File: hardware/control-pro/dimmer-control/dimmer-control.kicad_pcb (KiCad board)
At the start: 2 copper layers, 100 x 90 mm, 20 parts, among them J1 OUTPUT, J2 INPUT

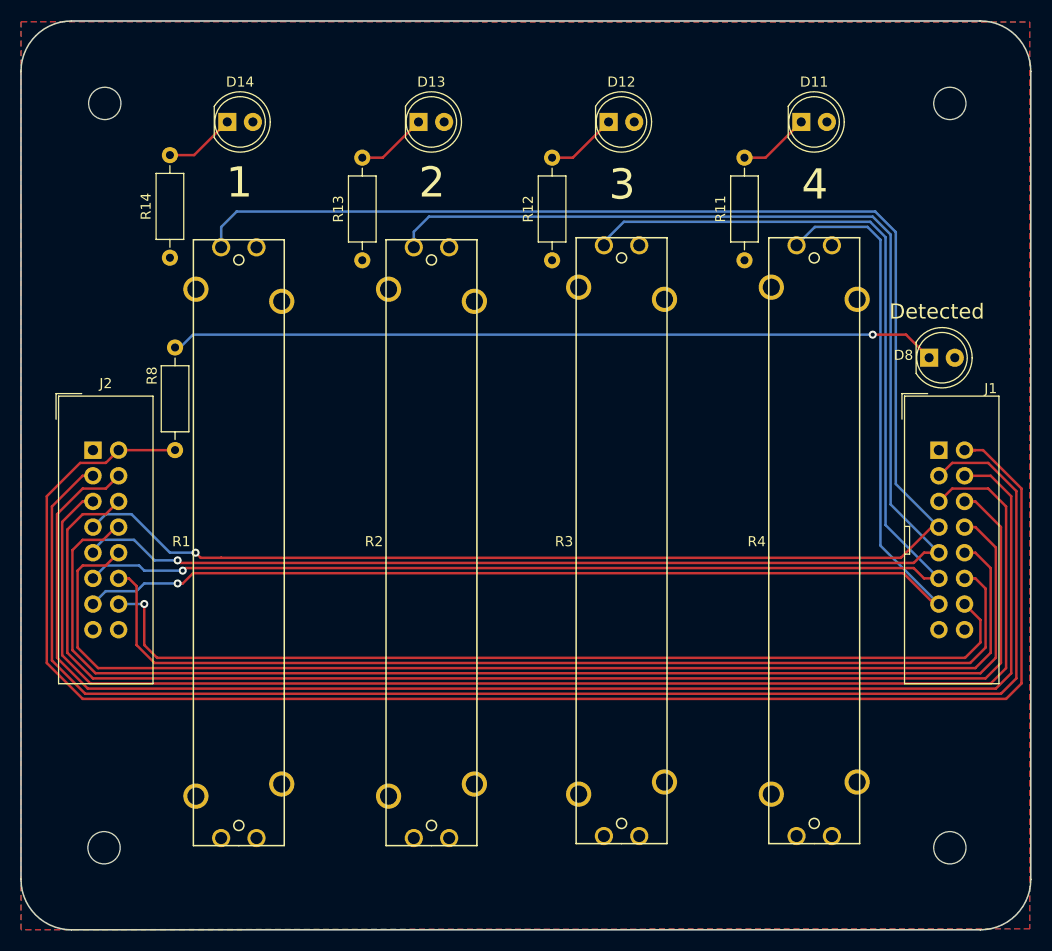
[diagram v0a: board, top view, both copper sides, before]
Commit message: TX2: - Added buffer to drive LEDs - Added decoupling capacitors - Fixed dimmer traces on PCB
DMX-CPC*:
- Switched to horizontal 16 pin connectors since vertical was too tall with a cable plugged in
- Swapped the clock speed and step switches to match the order on the TX1
- Swapped the data and clock LEDs to match the order on the TX1

DMX-CPD*:
- Split dimmer controls out to its own PCB
- Added 2nd 16 pin connector to daisy chain with DMX-CPC*.
- Switched to horizontal 16 pin connectors since vertical was too tall with a cable plugged in

Updated readmes with parts, board links.
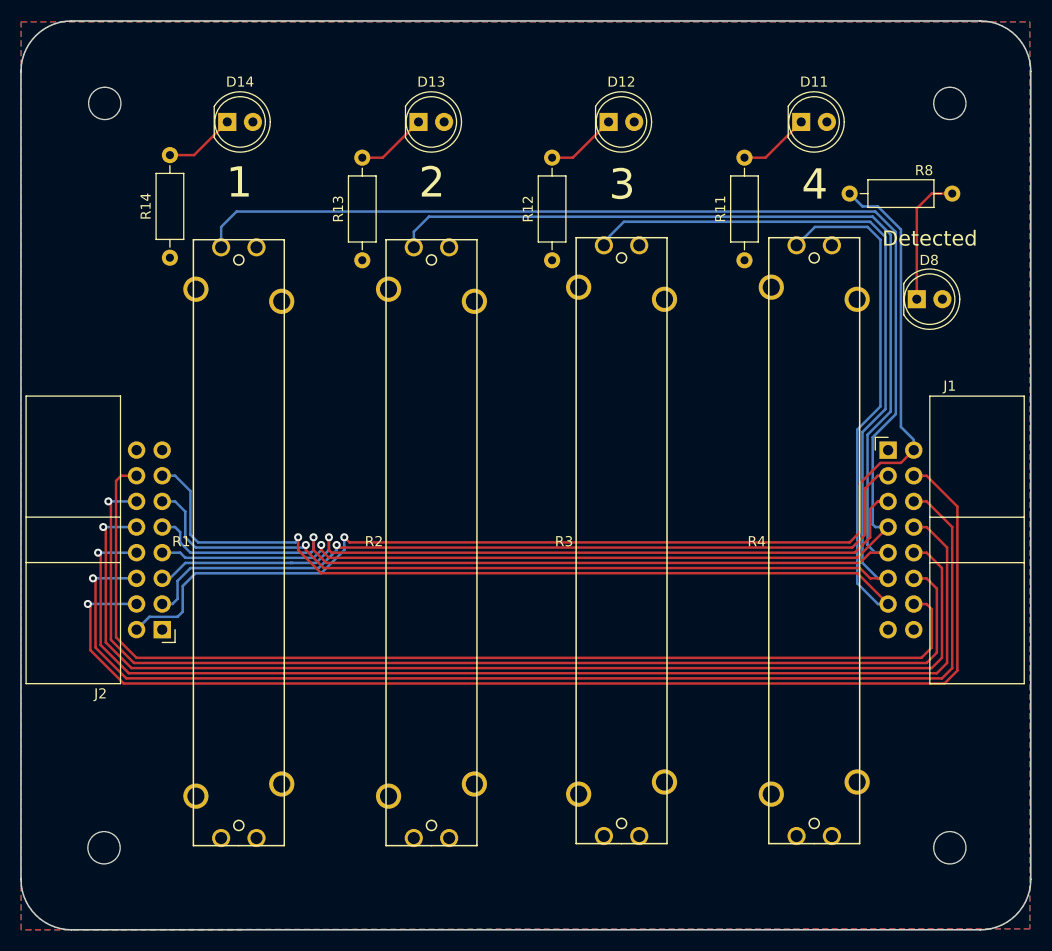
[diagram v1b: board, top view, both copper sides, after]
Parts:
- added ?: , footprints:OSHW-LOGO-S, B.Cu at (171.7, 135.9)
- added G***: LOGO, footprints:logo_cr_5x5, B.Cu at (149.7, 134.9)
- J1, J2: footprint Connector_IDC:IDC-Header_2x08_P2.54mm_Vertical -> Connector_IDC:IDC-Header_2x08_P2.54mm_Horizontal
- moved R8 71.5 mm to (169.2, 65.8), turned to 0 degrees
- moved J2 19.1 mm to (101.1, 109.0), turned to 180 degrees
- moved D8 5.93 mm to (175.8, 76.2)
- moved J1 5.03 mm to (173.0, 91.2)
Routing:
- net /~CLOCK: track 146.0 -> 81.4 mm, vias 0 -> 1
- net Net-(D8-Pad1): track 76.1 -> 13.1 mm, vias 1 -> 0
- net /~DATA: track 136.3 -> 80.2 mm, vias 0 -> 1
- net /~HWD_DT: track 157.5 -> 118.7 mm, vias 0 -> 1
- net /SPD_HI: track 141.3 -> 119.1 mm, vias 0 -> 1
- net /SPD_WIPER: track 130.7 -> 116.6 mm, vias 0 -> 1
- net /DIM1: track 188.6 -> 176.8 mm
- net /~CLK_FST: track 95.0 -> 105.6 mm, vias 1 -> 0
- net /SPD_LO: track 123.3 -> 114.0 mm, vias 0 -> 1
- net /DIM2: track 169.4 -> 161.3 mm
- net /DIM3: track 150.7 -> 143.1 mm
- net /~CLK_SLO: track 101.7 -> 108.8 mm, vias 0 -> 1
- net /DIM4: track 134.4 -> 129.4 mm
- net /~CLK_STEP: track 115.9 -> 111.4 mm, vias 0 -> 1
